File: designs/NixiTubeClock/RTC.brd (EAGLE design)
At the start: 160 x 100 mm, 7 parts, among them IC1 DS1307N+, U1 S8411-45R, Y1 CM7V-T1A-32.768K-9PF-20PPM-TA-

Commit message: updated RTC BRD
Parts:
- moved C1 26.9 mm to (16.5, 29.2)
- moved R1 19.8 mm to (6.35, 6.35), turned to 180 degrees
- moved R2 13.3 mm to (6.35, 10.2), turned to 180 degrees
- moved SV1 8.55 mm to (21.2, 14.6), turned to 90 degrees
- moved IC1 6.84 mm to (14.0, 20.3)
- moved Y1 6.84 mm to (6.35, 22.9)
- moved U1 0.62 mm to (8.52, 13.2), turned to 315 degrees
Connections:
- net SCL: now also SV1.2; no longer SV1.3
- net SDA: now also SV1.3; no longer SV1.4
- net SQW/OUT: now also SV1.1; no longer SV1.2
- net VCC: now also SV1.4; no longer SV1.1
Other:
- board size 160 x 100 mm -> 26 x 30.1 mm
- board text added: "RTC"

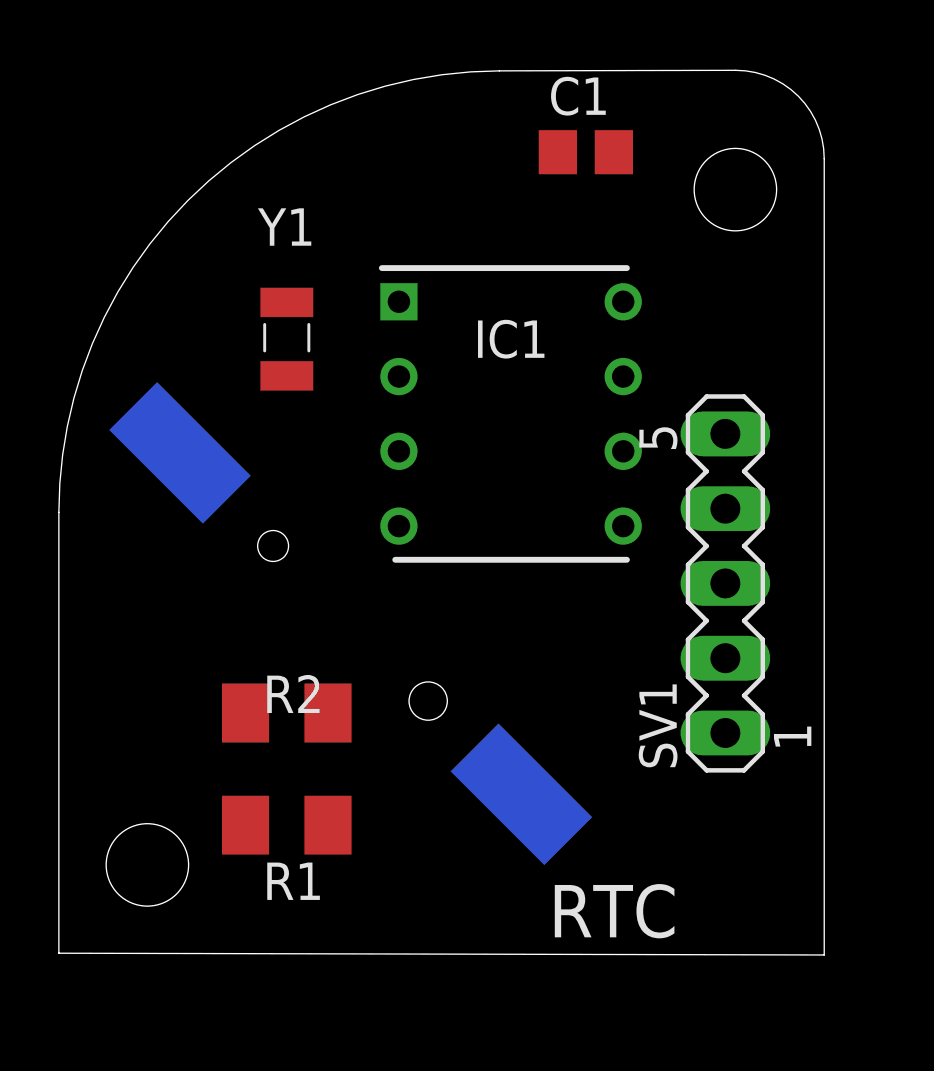
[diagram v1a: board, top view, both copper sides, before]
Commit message: finished RTC Brd
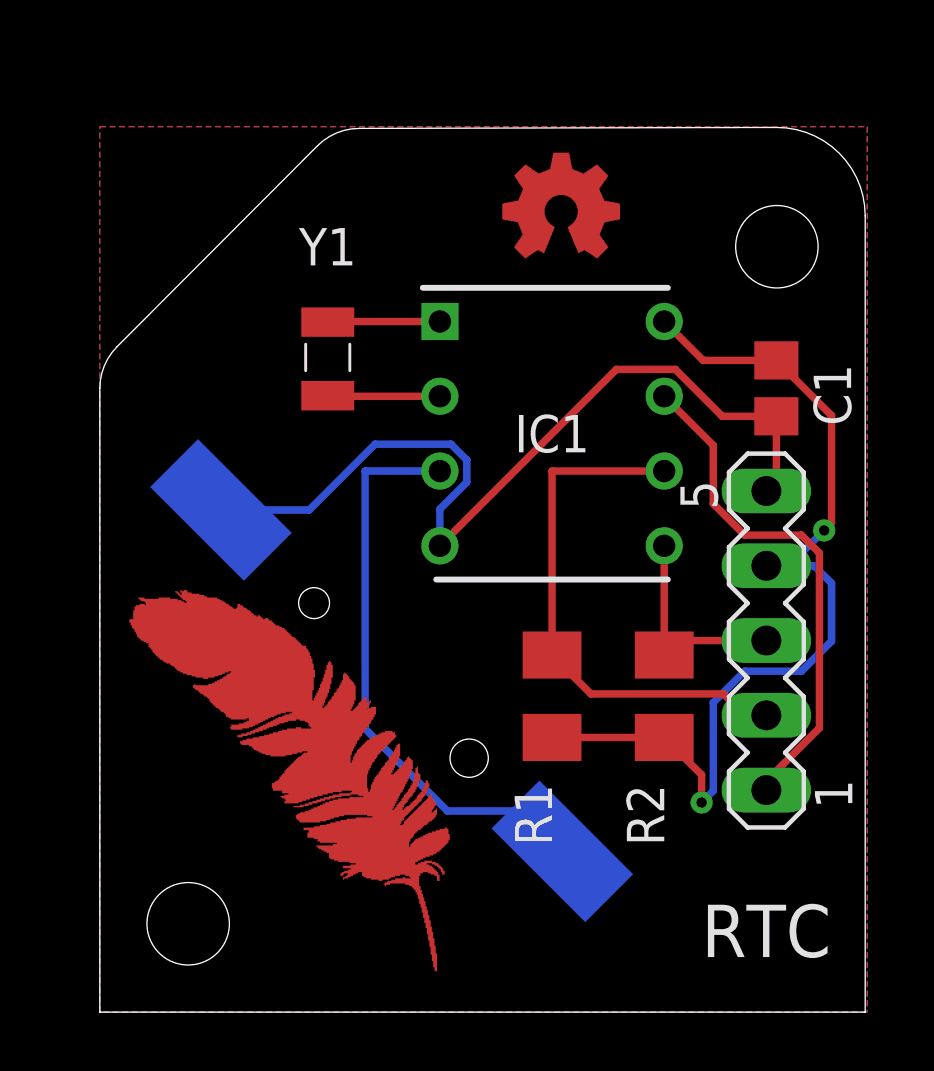
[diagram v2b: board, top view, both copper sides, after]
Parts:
- C1: value (none) -> 0.1uF
- R1, R2: value (none) -> 2.2K
- moved R2 12.8 mm to (19.2, 10.7), turned to 90 degrees
- moved C1 10.3 mm to (23.0, 21.2), turned to 90 degrees
- moved R1 10.0 mm to (15.4, 10.7), turned to 90 degrees
- moved SV1 2.39 mm to (22.6, 12.6)
- moved U1 2.39 mm to (9.91, 11.3)
- moved Y1 1.54 mm to (7.74, 22.2)
- moved IC1 1.54 mm to (15.4, 19.6)
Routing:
- net VCC: track 0.00 -> 32.9 mm, vias 0 -> 2
- net GND: track 0.00 -> 30.0 mm
- net VBAT: track 0.00 -> 19.7 mm
- net SCL: track 0.00 -> 18.2 mm
- net SQW/OUT: track 0.00 -> 17.4 mm
- net SDA: track 0.00 -> 7.38 mm
- net N$2: track 0.00 -> 3.82 mm
- net N$1: track 0.00 -> 3.82 mm
- added copper zone on layer 1, net GND
- added copper zone on layer 16, net GND
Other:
- outline, holes or cut-outs redrawn
